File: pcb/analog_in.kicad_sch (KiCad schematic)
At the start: 6 parts

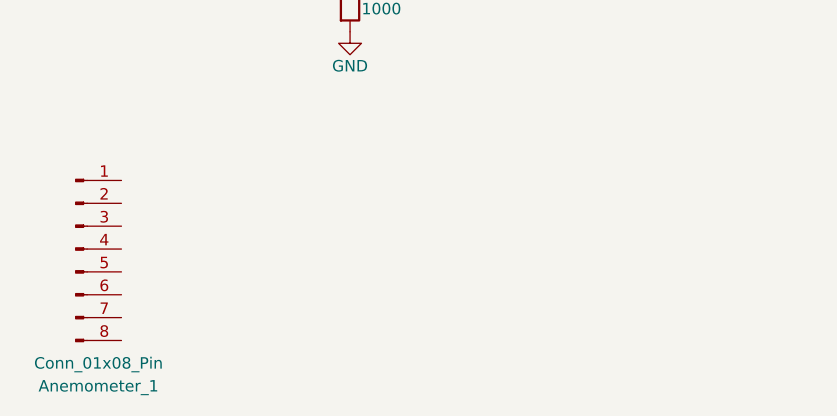
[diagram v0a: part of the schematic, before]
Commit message: added new sheet and added sensors
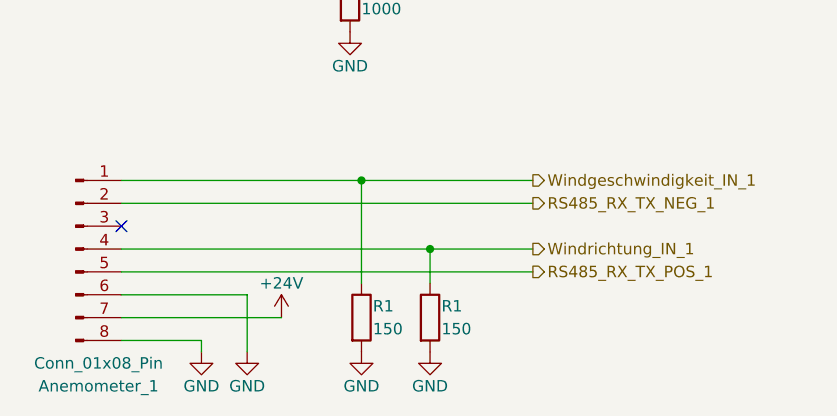
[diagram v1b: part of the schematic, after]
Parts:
- added R1 (x2): 150, Resistor_SMD:R_0201_0603Metric, symbol Device:R
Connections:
- net +24V: now also Anemometer_1.7 (Pin_7)
- net GND: now also Anemometer_1.6 (Pin_6), Anemometer_1.8 (Pin_8), R1.2, R1.2
- net Windgeschwindigkeit_IN_1: now reaches Anemometer_1.1 (Pin_1)
- net Windgeschwindigkeit_IN_1: now also R1.1
- net RS485_RX_TX_NEG_1: now reaches Anemometer_1.2 (Pin_2)
- net Windrichtung_IN_1: now reaches Anemometer_1.4 (Pin_4)
- net Windrichtung_IN_1: now also R1.1
- net RS485_RX_TX_POS_1: now reaches Anemometer_1.5 (Pin_5)
- no-connect marks 1 -> 2
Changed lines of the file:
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@@
 (kicad_sch (version 20230121) (generator eeschema)
   (paper "A4")
+  (junction (at 60.96 101.6) (diameter 0) (color 0 0 0 0)
+  )
   (junction (at 33.02 62.23) (diameter 0) (color 0 0 0 0)
   )
@@
   (junction (at 38.1 29.21) (diameter 0) (color 0 0 0 0)
   )
+  (junction (at 53.34 93.98) (diameter 0) (color 0 0 0 0)
+  )
+  (no_connect (at 26.67 99.06))
   (no_connect (at 26.67 24.13))
+  (wire (pts (xy 26.67 109.22) (xy 44.45 109.22))
+    (stroke (width 0) (type default))
+  )
   (wire (pts (xy 33.02 62.23) (xy 33.02 64.77))
     (stroke (width 0) (type default))
   )
+  (wire (pts (xy 40.64 106.68) (xy 40.64 113.03))
+    (stroke (width 0) (type default))
+  )
   (wire (pts (xy 38.1 35.56) (xy 38.1 36.83))
     (stroke (width 0) (type default))
@@
     (stroke (width 0) (type default))
   )
+  (wire (pts (xy 26.67 93.98) (xy 53.34 93.98))
+    (stroke (width 0) (type default))
+  )
+  (wire (pts (xy 53.34 93.98) (xy 53.34 105.41))
+    (stroke (width 0) (type default))
+  )
   (wire (pts (xy 41.91 62.23) (xy 41.91 66.04))
     (stroke (width 0) (type default))
@@
     (stroke (width 0) (type default))
   )
+  (wire (pts (xy 53.34 93.98) (xy 72.39 93.98))
+    (stroke (width 0) (type default))
+  )
+  (wire (pts (xy 26.67 104.14) (xy 72.39 104.14))
+    (stroke (width 0) (type default))
+  )
+  (wire (pts (xy 26.67 106.68) (xy 40.64 106.68))
+    (stroke (width 0) (type default))
+  )
   (wire (pts (xy 33.02 62.23) (xy 41.91 62.23))
     (stroke (width 0) (type default))
   )
+  (wire (pts (xy 35.56 111.76) (xy 35.56 113.03))
+    (stroke (width 0) (type default))
+  )
   (wire (pts (xy 52.07 67.31) (xy 52.07 68.58))
     (stroke (width 0) (type default))
   )
+  (wire (pts (xy 26.67 111.76) (xy 35.56 111.76))
+    (stroke (width 0) (type default))
+  )
   (wire (pts (xy 33.02 57.15) (xy 33.02 55.88))
     (stroke (width 0) (type default))
   )
+  (wire (pts (xy 60.96 101.6) (xy 60.96 105.41))
+    (stroke (width 0) (type default))
+  )
   (wire (pts (xy 26.67 57.15) (xy 33.02 57.15))
     (stroke (width 0) (type default))
   )
+  (wire (pts (xy 60.96 101.6) (xy 72.39 101.6))
+    (stroke (width 0) (type default))
+  )
   (wire (pts (xy 33.02 21.59) (xy 33.02 20.32))
     (stroke (width 0) (type default))
@@
     (stroke (width 0) (type default))
   )
+  (wire (pts (xy 26.67 96.52) (xy 72.39 96.52))
+    (stroke (width 0) (type default))
+  )
+  (wire (pts (xy 26.67 101.6) (xy 60.96 101.6))
+    (stroke (width 0) (type default))
+  )
   (wire (pts (xy 33.02 21.59) (xy 26.67 21.59))
     (stroke (width 0) (type default))
@@
   (wire (pts (xy 26.67 29.21) (xy 38.1 29.21))
     (stroke (width 0) (type default))
+  )
+  (hierarchical_label "RS485_RX_TX_NEG_1" (shape output) (at 72.39 96.52 0) (fields_autoplaced)
+    (effects (font (size 1.27 1.27)) (justify left))
+  )
+  (hierarchical_label "RS485_RX_TX_POS_1" (shape output) (at 72.39 104.14 0) (fields_autoplaced)
+    (effects (font (size 1.27 1.27)) (justify left))
+  )
+  (hierarchical_label "Windgeschwindigkeit_IN_1" (shape output) (at 72.39 93.98 0) (fields_autoplaced)
+    (effects (font (size 1.27 1.27)) (justify left))
+  )
+  (hierarchical_label "Windrichtung_IN_1" (shape output) (at 72.39 101.6 0) (fields_autoplaced)
+    (effects (font (size 1.27 1.27)) (justify left))
   )
   (hierarchical_label "Kraftmessung_IN_1" (shape output) (at 62.23 68.58 0) (fields_autoplaced)
@@
     (effects (font (size 1.27 1.27)) (justify left))
   )
+  (symbol (lib_id "Device:R") (at 60.96 109.22 0) (unit 1)
+    (in_bom yes) (on_board yes) (dnp no)
+    (property "Reference" "R1" (at 62.23 107.95 0)
+      (effects (font (size 1.27 1.27)) (justify left))
+    )
+    (property "Value" "150" (at 62.23 110.49 0)
+      (effects (font (size 1.27 1.27)) (justify left))
+    )
+    (property "Footprint" "Resistor_SMD:R_0201_0603Metric" (at 59.182 109.22 90)
+      (effects (font (size 1.27 1.27)) hide)
+    )
+    (property "Datasheet" "~" (at 60.96 109.22 0)
+      (effects (font (size 1.27 1.27)) hide)
+    )
+    (pin "1")
+    (pin "2")
+    (instances
+      (project "STM32_F439ZI_Shield"
+        (path "/19bff231-ff37-4a40-bd06-2039e9f55c77"
+          (reference "R1") (unit 1)
+        )
+        (path "/19bff231-ff37-4a40-bd06-2039e9f55c77/627cdbea-55a6-4b71-bf1e-ff5bf9a61719"
+          (reference "R5") (unit 1)
+        )
+      )
+    )
+  )
   (symbol (lib_id "power:GND") (at 38.1 35.56 0) (unit 1)
     (in_bom yes) (on_board yes) (dnp no)
@@
     )
   )
+  (symbol (lib_id "power:GND") (at 40.64 113.03 0) (unit 1)
+    (in_bom yes) (on_board yes) (dnp no)
+    (property "Reference" "#PWR014" (at 40.64 119.38 0)
+      (effects (font (size 1.27 1.27)) hide)
+    )
+    (property "Value" "GND" (at 40.64 116.84 0)
+      (effects (font (size 1.27 1.27)))
+    )
+    (property "Footprint" "" (at 40.64 113.03 0)
+      (effects (font (size 1.27 1.27)) hide)
+    )
+    (property "Datasheet" "" (at 40.64 113.03 0)
+      (effects (font (size 1.27 1.27)) hide)
+    )
+    (pin "1")
+    (instances
+      (project "STM32_F439ZI_Shield"
+        (path "/19bff231-ff37-4a40-bd06-2039e9f55c77/627cdbea-55a6-4b71-bf1e-ff5bf9a61719"
+          (reference "#PWR014") (unit 1)
+        )
+      )
+    )
+  )
   (symbol (lib_id "power:GND") (at 41.91 66.04 0) (unit 1)
     (in_bom yes) (on_board yes) (dnp no)
@@
         (path "/19bff231-ff37-4a40-bd06-2039e9f55c77/627cdbea-55a6-4b71-bf1e-ff5bf9a61719"
           (reference "#PWR010") (unit 1)
+        )
+      )
+    )
+  )
+  (symbol (lib_id "power:GND") (at 53.34 113.03 0) (unit 1)
+    (in_bom yes) (on_board yes) (dnp no)
+    (property "Reference" "#PWR016" (at 53.34 119.38 0)
+      (effects (font (size 1.27 1.27)) hide)
+    )
+    (property "Value" "GND" (at 53.34 116.84 0)
+      (effects (font (size 1.27 1.27)))
+    )
+    (property "Footprint" "" (at 53.34 113.03 0)
+      (effects (font (size 1.27 1.27)) hide)
+    )
+    (property "Datasheet" "" (at 53.34 113.03 0)
+      (effects (font (size 1.27 1.27)) hide)
+    )
+    (pin "1")
+    (instances
+      (project "STM32_F439ZI_Shield"
+        (path "/19bff231-ff37-4a40-bd06-2039e9f55c77/627cdbea-55a6-4b71-bf1e-ff5bf9a61719"
+          (reference "#PWR016") (unit 1)
         )
       )
@@
         (path "/19bff231-ff37-4a40-bd06-2039e9f55c77/627cdbea-55a6-4b71-bf1e-ff5bf9a61719"
           (reference "Kraftsensor_1") (unit 1)
+        )
+      )
+    )
+  )
+  (symbol (lib_id "power:GND") (at 60.96 113.03 0) (unit 1)
+    (in_bom yes) (on_board yes) (dnp no)
+    (property "Reference" "#PWR017" (at 60.96 119.38 0)
+      (effects (font (size 1.27 1.27)) hide)
+    )
+    (property "Value" "GND" (at 60.96 116.84 0)
+      (effects (font (size 1.27 1.27)))
+    )
+    (property "Footprint" "" (at 60.96 113.03 0)
+      (effects (font (size 1.27 1.27)) hide)
+    )
+    (property "Datasheet" "" (at 60.96 113.03 0)
+      (effects (font (size 1.27 1.27)) hide)
+    )
+    (pin "1")
+    (instances
+      (project "STM32_F439ZI_Shield"
+        (path "/19bff231-ff37-4a40-bd06-2039e9f55c77/627cdbea-55a6-4b71-bf1e-ff5bf9a61719"
+          (reference "#PWR017") (unit 1)
         )
       )
@@
         )
       )
+    )
+  )
+  (symbol (lib_id "power:GND") (at 35.56 113.03 0) (unit 1)
+    (in_bom yes) (on_board yes) (dnp no)
+    (property "Reference" "#PWR013" (at 35.56 119.38 0)
+      (effects (font (size 1.27 1.27)) hide)
+    )
+    (property "Value" "GND" (at 35.56 116.84 0)
+      (effects (font (size 1.27 1.27)))
+    )
+    (property "Footprint" "" (at 35.56 113.03 0)
+      (effects (font (size 1.27 1.27)) hide)
+    )
+    (property "Datasheet" "" (at 35.56 113.03 0)
+      (effects (font (size 1.27 1.27)) hide)
+    )
+    (pin "1")
+    (instances
+      (project "STM32_F439ZI_Shield"
+        (path "/19bff231-ff37-4a40-bd06-2039e9f55c77/627cdbea-55a6-4b71-bf1e-ff5bf9a61719"
+          (reference "#PWR013") (unit 1)
+        )
+      )
+    )
+  )
+  (symbol (lib_id "power:+24V") (at 44.45 109.22 0) (unit 1)
+    (in_bom yes) (on_board yes) (dnp no) (fields_autoplaced)
+    (property "Reference" "#PWR015" (at 44.45 113.03 0)
+      (effects (font (size 1.27 1.27)) hide)
+    )
+    (property "Value" "+24V" (at 44.45 105.41 0)
+      (effects (font (size 1.27 1.27)))
+    )
+    (property "Footprint" "" (at 44.45 109.22 0)
+      (effects (font (size 1.27 1.27)) hide)
+    )
+    (property "Datasheet" "" (at 44.45 109.22 0)
+      (effects (font (size 1.27 1.27)) hide)
+    )
+    (pin "1")
+    (instances
+      (project "STM32_F439ZI_Shield"
+        (path "/19bff231-ff37-4a40-bd06-2039e9f55c77/627cdbea-55a6-4b71-bf1e-ff5bf9a61719"
+          (reference "#PWR015") (unit 1)
+        )
+      )
+    )
+  )
+  (symbol (lib_id "Device:R") (at 53.34 109.22 0) (unit 1)
+    (in_bom yes) (on_board yes) (dnp no)
+    (property "Reference" "R1" (at 54.61 107.95 0)
+      (effects (font (size 1.27 1.27)) (justify left))
+    )
+    (property "Value" "150" (at 54.61 110.49 0)
+      (effects (font (size 1.27 1.27)) (justify left))
+    )
+    (property "Footprint" "Resistor_SMD:R_0201_0603Metric" (at 51.562 109.22 90)
+      (effects (font (size 1.27 1.27)) hide)
+    )
+    (property "Datasheet" "~" (at 53.34 109.22 0)
+      (effects (font (size 1.27 1.27)) hide)
+    )
+    (pin "1")
+    (pin "2")
+    (instances
+      (project "STM32_F439ZI_Shield"
+        (path "/19bff231-ff37-4a40-bd06-2039e9f55c77"
+          (reference "R1") (unit 1)
+        )
+        (path "/19bff231-ff37-4a40-bd06-2039e9f55c77/627cdbea-55a6-4b71-bf1e-ff5bf9a61719"
+          (reference "R4") (unit 1)
+        )
+      )

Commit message: Updated footprints
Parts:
- Abstandssensor_1: footprint Connector:FanPinHeader_1x04_P2.54mm_Vertical -> Connector_Phoenix_MSTB:PhoenixContact_MSTBA_2,5_4-G-5,08_1x04_P5.08mm_Horizontal
- Anemometer_1: footprint (none) -> Connector_Phoenix_MSTB:PhoenixContact_MSTBA_2,5_8-G-5,08_1x08_P5.08mm_Horizontal
- Kraftsensor_1: footprint (none) -> Connector_Phoenix_MSTB:PhoenixContact_MSTBA_2,5_4-G-5,08_1x04_P5.08mm_Horizontal
- R1: footprint Resistor_SMD:R_0201_0603Metric -> Resistor_SMD:R_1206_3216Metric
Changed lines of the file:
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@@
       (effects (font (size 1.27 1.27)) (justify left))
     )
-    (property "Footprint" "Resistor_SMD:R_0201_0603Metric" (at 59.182 109.22 90)
+    (property "Footprint" "Resistor_SMD:R_1206_3216Metric" (at 59.182 109.22 90)
       (effects (font (size 1.27 1.27)) hide)
     )
@@
       (effects (font (size 1.27 1.27)))
     )
-    (property "Footprint" "" (at 21.59 59.69 0)
+    (property "Footprint" "Connector_Phoenix_MSTB:PhoenixContact_MSTBA_2,5_4-G-5,08_1x04_P5.08mm_Horizontal" (at 21.59 59.69 0)
       (effects (font (size 1.27 1.27)) hide)
     )
@@
       (effects (font (size 1.27 1.27)))
     )
-    (property "Footprint" "" (at 21.59 101.6 0)
+    (property "Footprint" "Connector_Phoenix_MSTB:PhoenixContact_MSTBA_2,5_8-G-5,08_1x08_P5.08mm_Horizontal" (at 21.59 101.6 0)
       (effects (font (size 1.27 1.27)) hide)
     )
@@
       (effects (font (size 1.27 1.27)) (justify left))
     )
-    (property "Footprint" "Resistor_SMD:R_0201_0603Metric" (at 50.292 63.5 90)
+    (property "Footprint" "Resistor_SMD:R_1206_3216Metric" (at 50.292 63.5 90)
       (effects (font (size 1.27 1.27)) hide)
     )
@@
       (effects (font (size 1.27 1.27)) (justify left))
     )
-    (property "Footprint" "Resistor_SMD:R_0201_0603Metric" (at 36.322 33.02 90)
+    (property "Footprint" "Resistor_SMD:R_1206_3216Metric" (at 36.322 33.02 90)
       (effects (font (size 1.27 1.27)) hide)
     )
@@
       (effects (font (size 1.27 1.27)) (justify left))
     )
-    (property "Footprint" "Resistor_SMD:R_0201_0603Metric" (at 50.292 73.66 90)
+    (property "Footprint" "Resistor_SMD:R_1206_3216Metric" (at 50.292 73.66 90)
       (effects (font (size 1.27 1.27)) hide)
     )
@@
       (effects (font (size 1.27 1.27)))
     )
-    (property "Footprint" "Connector:FanPinHeader_1x04_P2.54mm_Vertical" (at 21.59 24.13 0)
+    (property "Footprint" "Connector_Phoenix_MSTB:PhoenixContact_MSTBA_2,5_4-G-5,08_1x04_P5.08mm_Horizontal" (at 21.59 24.13 0)
       (effects (font (size 1.27 1.27)) hide)
     )
@@
       (effects (font (size 1.27 1.27)) (justify left))
     )
-    (property "Footprint" "Resistor_SMD:R_0201_0603Metric" (at 51.562 109.22 90)
-      (effects (font (size 1.27 1.27)) hide)
-    )
+    (property "Footprint" "Resistor_SMD:R_1206_3216Metric" (at 51.562 109.22 90)
+      (effects (font (size 1.27 1.27)) hide)
+    )

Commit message: updated pcb
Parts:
- removed Abstandssensor_1: Conn_01x04_Pin, Connector_Phoenix_MSTB:PhoenixContact_MSTBA_2,5_4-G-5,08_1x04_P5.08mm_Horizontal, symbol Connector:Conn_01x04_Pin
- removed Anemometer_1: Conn_01x08_Pin, Connector_Phoenix_MSTB:PhoenixContact_MSTBA_2,5_8-G-5,08_1x08_P5.08mm_Horizontal, symbol Connector:Conn_01x08_Pin
- removed R1: 2300, Resistor_SMD:R_1206_3216Metric, symbol Device:R
- removed R1: 1000, Resistor_SMD:R_1206_3216Metric, symbol Device:R
- added Abstandssensor1: Conn_01x03_Pin, TerminalBlock_TE-Connectivity:TerminalBlock_TE_282834-3_1x03_P2.54mm_Horizontal, symbol Connector:Conn_01x03_Pin
- added Anenometer1: Conn_01x07_Pin, TerminalBlock_TE-Connectivity:TerminalBlock_TE_282834-7_1x07_P2.54mm_Horizontal, symbol Connector:Conn_01x07_Pin
- added R1: 1000, Resistor_SMD:R_1206_3216Metric, symbol Device:R
- added R1: 2300, Resistor_SMD:R_1206_3216Metric, symbol Device:R
- Kraftmessung1: renamed from Kraftsensor_1; footprint Connector_Phoenix_MSTB:PhoenixContact_MSTBA_2,5_4-G-5,08_1x04_P5.08mm_Horizontal -> TerminalBlock_TE-Connectivity:TerminalBlock_TE_282834-3_1x03_P2.54mm_Horizontal; symbol Connector:Conn_01x04_Pin -> Connector:Conn_01x03_Pin
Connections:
- net +24V: now also Abstandssensor1.1 (Pin_1), Anenometer1.1 (Pin_1)
- net Abstandsmessung_IN_1: now also Abstandssensor1.3 (Pin_3)
- net GND: now also Kraftmessung1.2 (Pin_2), Abstandssensor1.2 (Pin_2), Anenometer1.2 (Pin_2), Anenometer1.5 (Pin_5), R1.2; no longer Kraftmessung1.3 (Pin_3), Kraftmessung1.4 (Pin_4)
- net Kraftmessung_IN_1: now also R1.1, R1.1
- net RS485_RX_TX_NEG_1: now also Anenometer1.3 (Pin_3)
- net RS485_RX_TX_POS_1: now also Anenometer1.4 (Pin_4)
- net Windgeschwindigkeit_IN_1: now also Anenometer1.7 (Pin_7)
- net Windrichtung_IN_1: now also Anenometer1.6 (Pin_6)
- new net: Kraftmessung1.3 (Pin_3), R1.2
- no-connect marks 2 -> 0
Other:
- moved on the sheet: R1

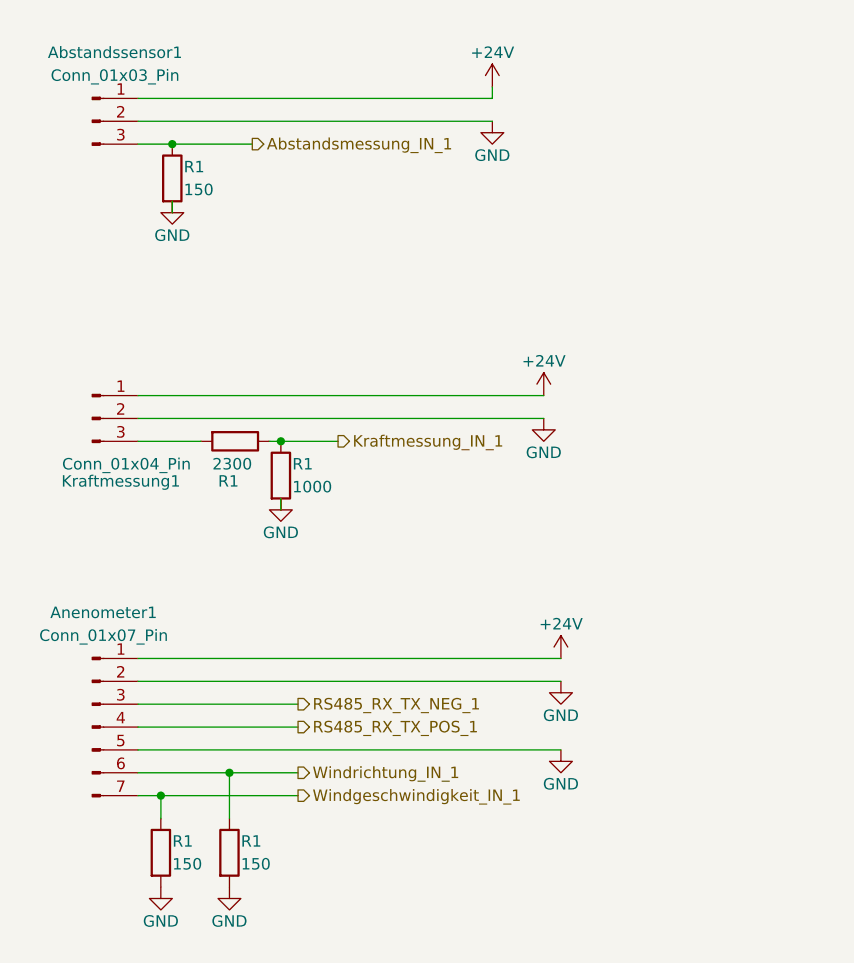
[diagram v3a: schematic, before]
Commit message: finished assigning pins and creating pcb
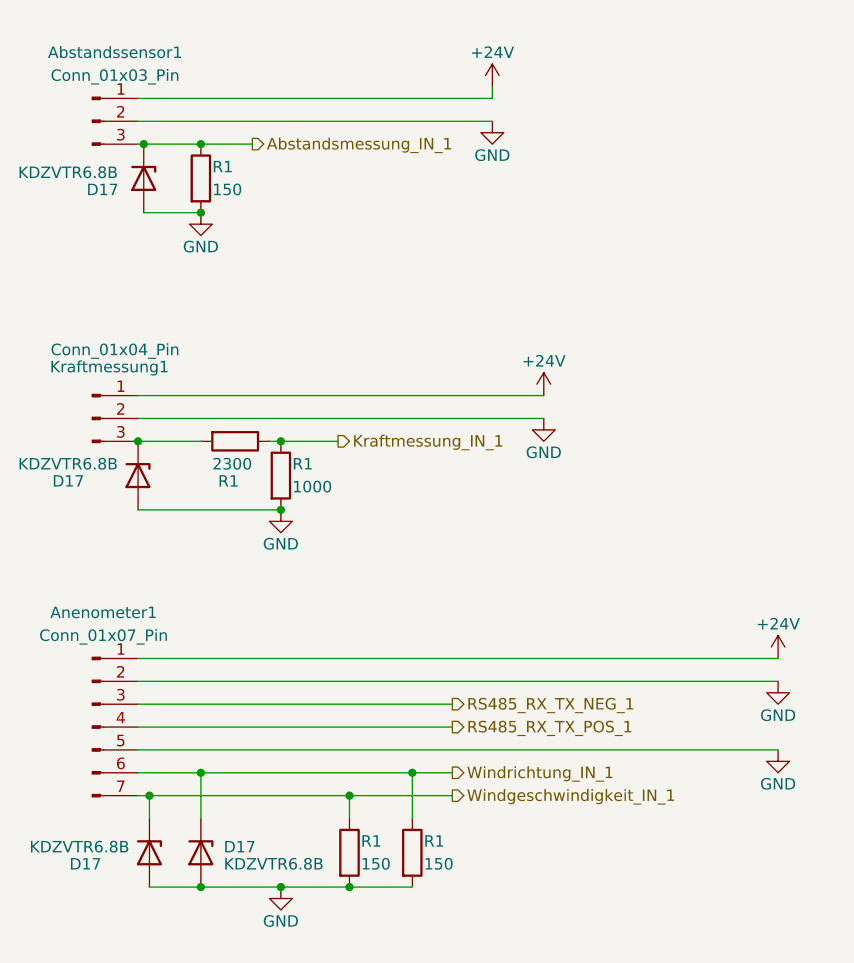
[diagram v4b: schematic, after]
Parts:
- added D17 (x4): KDZVTR6.8B, Diode_SMD:D_SOD-123, symbol Diode:Z2SMBxxx
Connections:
- net Abstandsmessung_IN_1: now also D17.1 (K)
- net GND: now also D17.2 (A), D17.2 (A), D17.2 (A), D17.2 (A)
- net Windgeschwindigkeit_IN_1: now also D17.1 (K)
- net Windrichtung_IN_1: now also D17.1 (K)
- net at Kraftmessung1.3 (Pin_3), R1.2: now also D17.1 (K)
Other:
- moved on the sheet: R1
